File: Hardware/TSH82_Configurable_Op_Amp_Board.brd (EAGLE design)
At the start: 22.9 x 25.4 mm, 76 parts, among them U1 TSH82

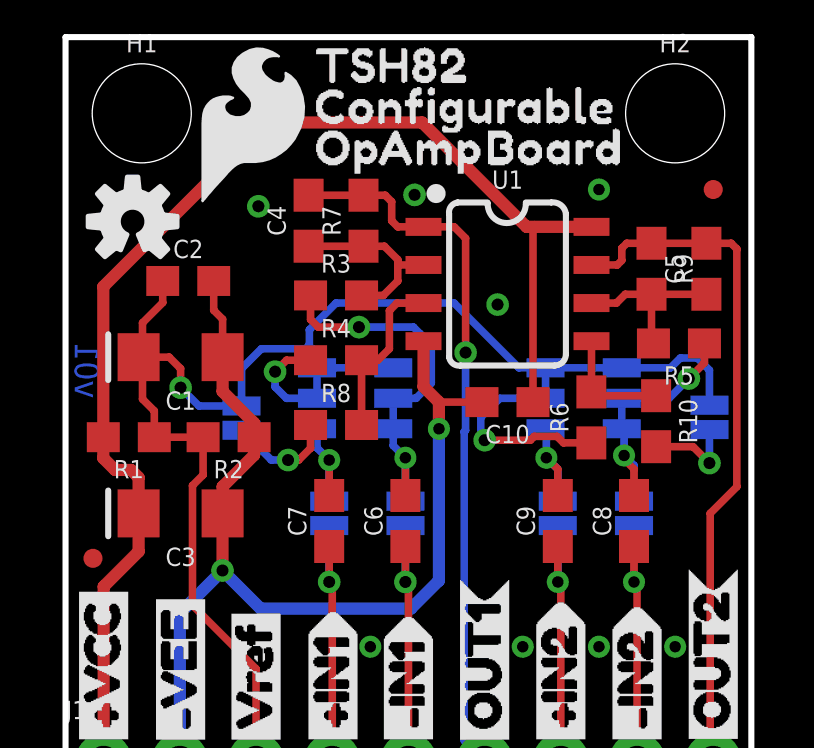
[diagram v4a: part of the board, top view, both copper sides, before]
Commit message: Add bottom fiducials, move a trace, increment version, remove extra files.
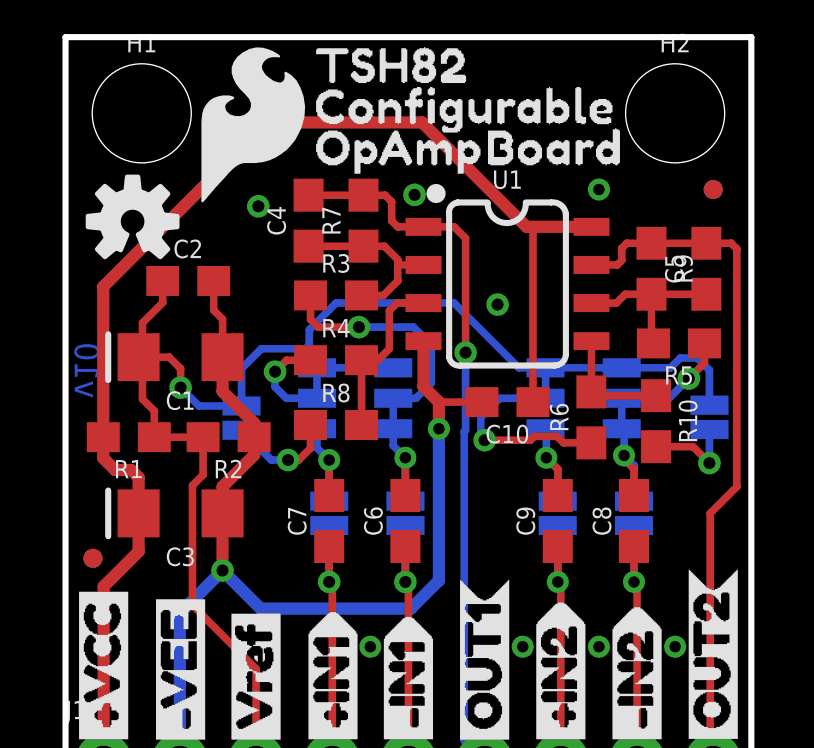
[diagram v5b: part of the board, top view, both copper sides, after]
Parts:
- added FD3, FD4: FIDUCIALUFIDUCIAL, SparkFun-Aesthetics:FIDUCIAL-MICRO
- U1: device pete:SO08 -> SparkFun-IC-Amplifiers:SO08
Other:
- board text added: "v10"
- board text removed: "v01"
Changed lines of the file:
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@@
 <wire x1="22.86" y1="25.4" x2="0" y2="25.4" width="0.2032" layer="20"/>
 <wire x1="0" y1="25.4" x2="0" y2="0" width="0.2032" layer="20"/>
-<text x="0.3048" y="13.3604" size="0.8128" layer="16" font="vector" ratio="15" rot="MR90">v01</text>
+<text x="0.3048" y="13.3604" size="0.8128" layer="16" font="vector" ratio="15" rot="MR90">v10</text>
 <text x="17.78" y="-10.16" size="1.778" layer="51" font="vector">Pete Dokter</text>
 <dimension x1="0" y1="25.4" x2="22.86" y2="25.4" x3="11.43" y3="31.75" textsize="1.778" layer="47" dtype="horizontal" unit="inch"/>
@@
 <attribute name="PROD_ID" value="RES-07871" x="19.5326" y="17.6784" size="1.778" layer="27" rot="R270" display="off"/>
 </element>
-<element name="U1" library="pete" package="SO08" value="TSH82" x="14.732" y="17.1704" rot="R270"/>
+<element name="U1" library="SparkFun-IC-Amplifiers" package="SO08" value="TSH82" x="14.732" y="17.1704" rot="R270"/>
 <element name="H1" library="SparkFun-Hardware" package="STAND-OFF" value="STAND-OFF" x="2.54" y="22.86"/>
 <element name="H2" library="SparkFun-Hardware" package="STAND-OFF" value="STAND-OFF" x="20.32" y="22.86"/>
@@
 <element name="U$35" library="buzzard_labels (6)" package="JP98" value="" x="7.3914" y="14.3764" rot="MR0"/>
 <element name="U$36" library="buzzard_labels (6)" package="JP109" value="" x="23.2664" y="14.859" rot="MR0"/>
+<element name="FD3" library="SparkFun-Aesthetics" package="FIDUCIAL-MICRO" value="FIDUCIALUFIDUCIAL" x="0.9144" y="8.0264" rot="MR0"/>
+<element name="FD4" library="SparkFun-Aesthetics" package="FIDUCIAL-MICRO" value="FIDUCIALUFIDUCIAL" x="21.59" y="20.32" rot="MR0"/>
 </elements>
 <signals>
